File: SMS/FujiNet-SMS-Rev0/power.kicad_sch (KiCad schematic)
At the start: 15 parts, among them Q2 AO3401A, U12 AP63203WU, U13 AP2112K-3.3

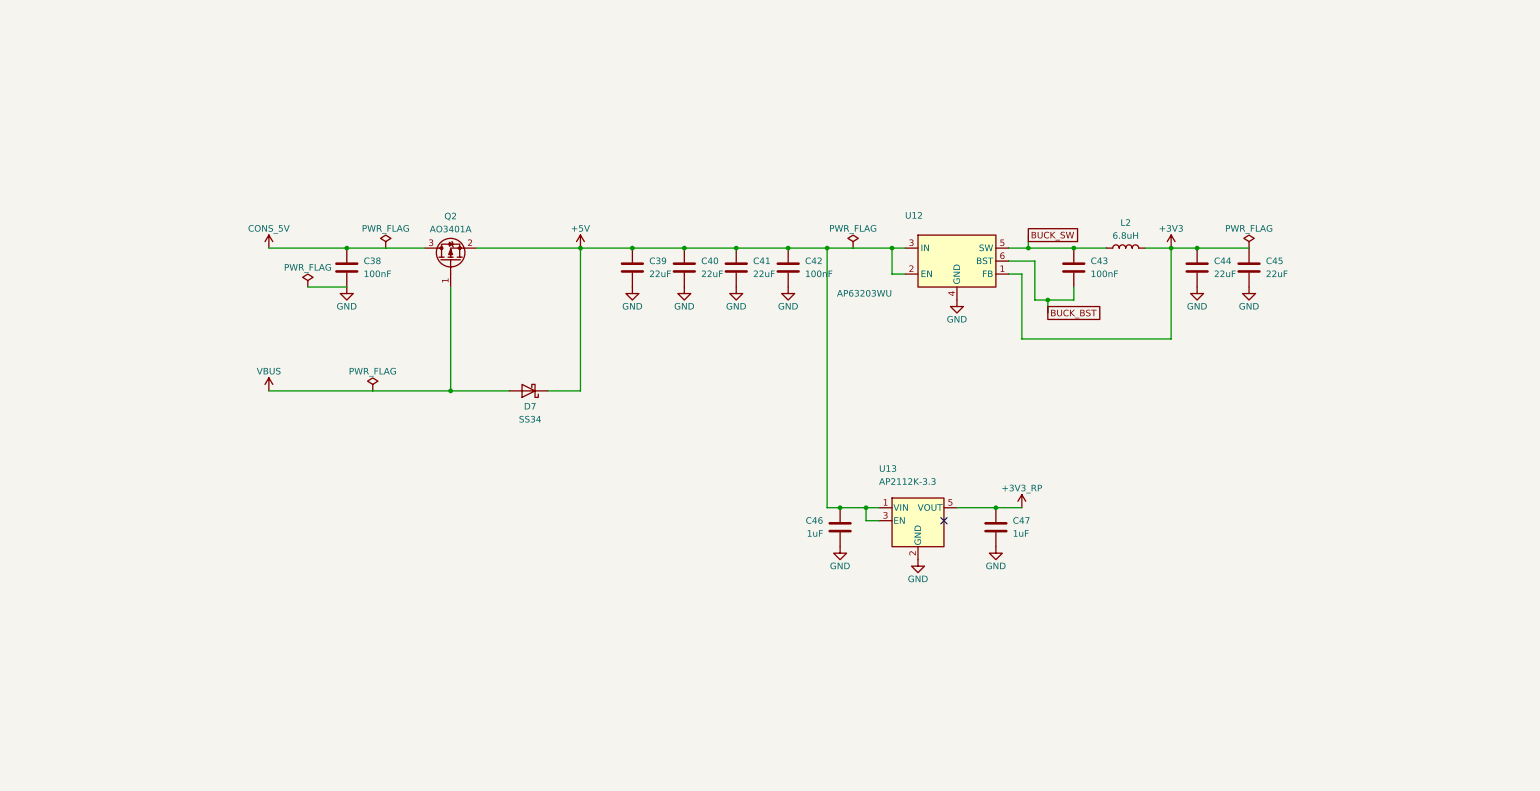
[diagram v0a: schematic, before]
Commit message: SMS Rev0: co-designed 6-layer board, board-mirroring schematic, JLCPCB + PCBWay packages (#52)
* SMS Rev0: audit with kicad-happy + datasheets, fix the edge, redraw the schematic

Edge connector: every source (SMS Power slot diagram, little-scale, a 171-5519
scan, raphnet, the barbeque and reidrac footprints) puts the EVEN pins on the
component / label side with pins 1/2 at the right.  The schematic-only
footprint had the faces swapped, which would have put console +5V on /WR.
make_edge_fp.py now writes even pads on F.Cu, odd on B.Cu, 1.75 x 8.75 mm
fingers 0.75-9.5 mm from the edge on a 65.8 mm tab; check_nets.py asserts it
and tools/audit/edge_orientation.py checks it against the sources.

kicad-happy + datasheet audit (docs/design-review-rev0.md Part 1, 27 deep
review findings, gate 27/27): R_VBPD 4.7k VBUS pull-down (SS34 leakage lifts
the P-FET gate), /WAIT gate pull-up 10k -> 4.7k (GPIO34's reset pull-down vs
the 2N7002's 2.5 V threshold), 10 uF bulk on the console 5V.

Schematic: hierarchical sheets wired on a root block diagram (edge -> RP2354B
-> ESP32-S3 -> USB, glue and SRAM under the RP, power below); every sheet
drawn left to right, the glue as a wired logic network by gate depth, the
RP2354B mirrored so its bus faces the console, small sheets on A4.  Parts
are addressed by key (design.py), no more NES reference aliasing.  sch_draw
gains hierarchical labels, sheet blocks, a bus graph and flag / power-pin
lints; gen_sch checks the hierarchy against design.py and names nets by
their last path element (one bus vector per bus: KiCad joins differing
vectors by position).  ERC 0, check_nets 437/437, check_glue 8192/8192.

JLC CPL rotations measured against the EasyEDA footprint of every LCSC part
(tools/audit/jlc); the AS6C4008 has no EasyEDA footprint.

Co-Authored-By: Claude Opus 5.5 <noreply@anthropic.com>

* SMS Rev0: board pipeline, placement and cartridge shell (WIP, not routed yet)

The NES Rev0 6-layer pipeline ported to SMS (gen_pcb, fanout, Freerout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
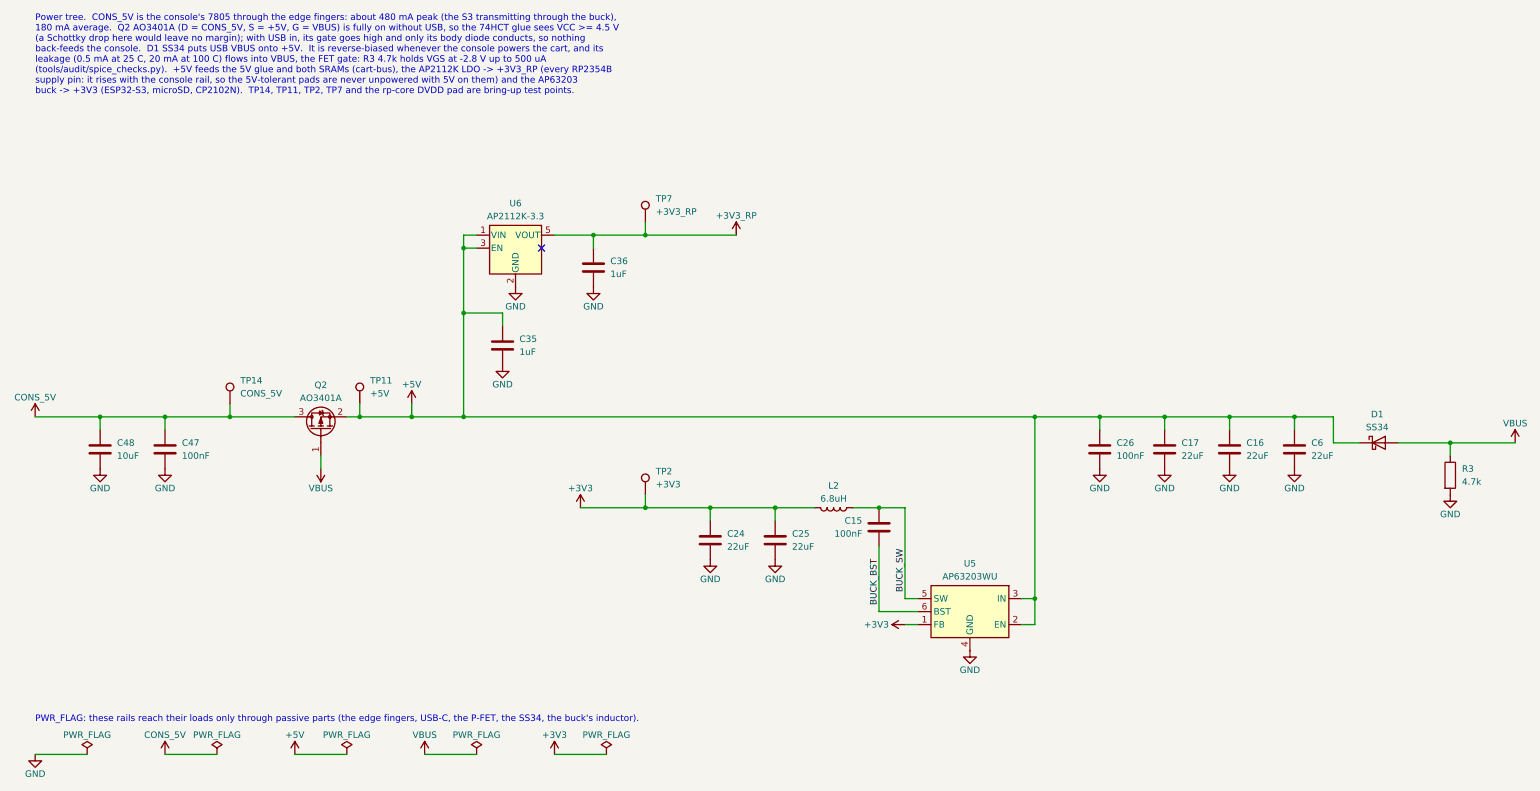
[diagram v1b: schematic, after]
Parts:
- removed C38, C42, C43: 100nF, FujiNet-SMS:C_0603_1608Metric, symbol Device:C
- removed C39, C40, C41, C44, C45: 22uF, FujiNet-SMS:C_0805_2012Metric, symbol Device:C
- removed C46: 1uF, FujiNet-SMS:C_0603_1608Metric, symbol Device:C
- removed D7: SS34, FujiNet-SMS:D_SMA, symbol Diode:SS34
- removed U12: AP63203WU, FujiNet-SMS:TSOT-23-6, symbol Regulator_Switching:AP63203WU
- removed U13: AP2112K-3.3, FujiNet-SMS:SOT-23-5, symbol Regulator_Linear:AP2112K-3.3
- added C15, C26: 100nF, FujiNet-SMS:C_0603_1608Metric, symbol Device:C
- added C16, C17, C24, C25, C6: 22uF, FujiNet-SMS:C_0805_2012Metric, symbol Device:C
- added C35, C36: 1uF, FujiNet-SMS:C_0603_1608Metric, symbol Device:C
- added C48: 10uF, FujiNet-SMS:C_0603_1608Metric, symbol Device:C
- added D1: SS34, FujiNet-SMS:D_SMA, symbol Diode:SS34
- added R3: 4.7k, FujiNet-SMS:R_0603_1608Metric, symbol Device:R
- added TP11: +5V, FujiNet-SMS:TestPoint_Pad_D1.5mm, symbol Connector:TestPoint
- added TP14: CONS_5V, FujiNet-SMS:TestPoint_Pad_D1.5mm, symbol Connector:TestPoint
- added TP2: +3V3, FujiNet-SMS:TestPoint_Pad_D1.5mm, symbol Connector:TestPoint
- added TP7: +3V3_RP, FujiNet-SMS:TestPoint_Pad_D1.5mm, symbol Connector:TestPoint
- added U5: AP63203WU, FujiNet-SMS:TSOT-23-6, symbol Regulator_Switching:AP63203WU
- added U6: AP2112K-3.3, FujiNet-SMS:SOT-23-5, symbol Regulator_Linear:AP2112K-3.3
- C47: value 1uF -> 100nF; LCSC C15849 -> C14663; MPN CL10A105KB8NNNC -> CC0603KRX7R9BB104; Manufacturer (none) -> YAGEO
- L2: Manufacturer (none) -> Sunlord
- Q2: Manufacturer (none) -> Alpha & Omega Semiconductor
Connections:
- net +3V3: now also C24.1, C25.1, TP2.1, U5.1 (FB)
- net +3V3_RP: now also C36.1, TP7.1, U6.5 (VOUT); no longer C47.1
- net +5V: now also C16.1, C17.1, C26.1, C35.1, C6.1, D1.1 (K), TP11.1, U5.2 (EN), U5.3 (IN), U6.1 (VIN), U6.3 (EN)
- net BUCK_BST: now also C15.2, U5.6 (BST)
- net BUCK_SW: now also C15.1, U5.5 (SW)
- net CONS_5V: now also C47.1, C48.1, TP14.1
- net GND: now also C16.2, C17.2, C24.2, C25.2, C26.2, C35.2, C36.2, C48.2, C6.2, R3.2, U5.4 (GND), U6.2 (GND)
- net VBUS: now also D1.2 (A), R3.1
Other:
- note added: "PWR_FLAG: these rails reach their loads only through passive parts (the edge fingers, USB-C, the P-FET, the SS34, the buck's inductor)."
- note added: "Power tree. CONS_5V is the console's 7805 through the edge fingers: about 480 mA peak (the S3 transmitting through the buck), 180 mA average. Q2 AO3401A (D = CONS_5V, S = +5V, G = VBUS) is fully on without USB, so the 74HCT glue sees VCC >= 4.5 V (a Schottky drop here would leave no margin); with USB in, its gate goes high and only its body diode conducts, so nothing back-feeds the console. D1 SS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"
- moved on the sheet: C47, L2, Q2
